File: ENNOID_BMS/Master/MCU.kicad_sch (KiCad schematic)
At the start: 36 parts, among them J17 DEBUG, Q27 BSS138, U11 LTC6820, U17 STM32F303CCTx, U2 LTC6820, Y1 8MHz

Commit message: ENNOID BMS PCBs completed
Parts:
- Q27: footprint TO_SOT_Packages_SMD:SOT-23 -> Package_TO_SOT_SMD:SOT-23
- U11, U2: footprint Housings_SSOP:MSOP-16_3x4mm_Pitch0.5mm -> Package_SO:MSOP-16_3x4.039mm_P0.5mm
- U17: footprint Housings_QFP:LQFP-48_7x7mm_Pitch0.5mm -> Package_QFP:LQFP-48_7x7mm_P0.5mm
- Y1: footprint Crystals:Crystal_SMD_Abracon_ABM3-2pin_5.0x3.2mm -> Crystal:Crystal_SMD_Abracon_ABM3-2Pin_5.0x3.2mm
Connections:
- net CS_TEMP: now reaches U17.25 (PB12/ADC4_IN3/COMP3_INM/I2C2_SMBA/I2S2_WS/OPAMP4_VOUT/SPI2_NSS/TIM1_BKIN/TSC_G6_IO2/USART3_CK)
- net CS_TEMP: now also U11.5 (CSB)
- net MA renamed MA_CELL
- net MA_CELL: no longer TR4.6
- net PA renamed PA_CELL
- net PA_CELL: no longer TR4.4
- net SS renamed CS_CELL
- net CS_CELL: no longer U11.5 (CSB)
- new net MA_TEMP: TR4.6
- new net PA_TEMP: TR4.4
- no-connect marks 5 -> 4
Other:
- moved on the sheet: R37, R51

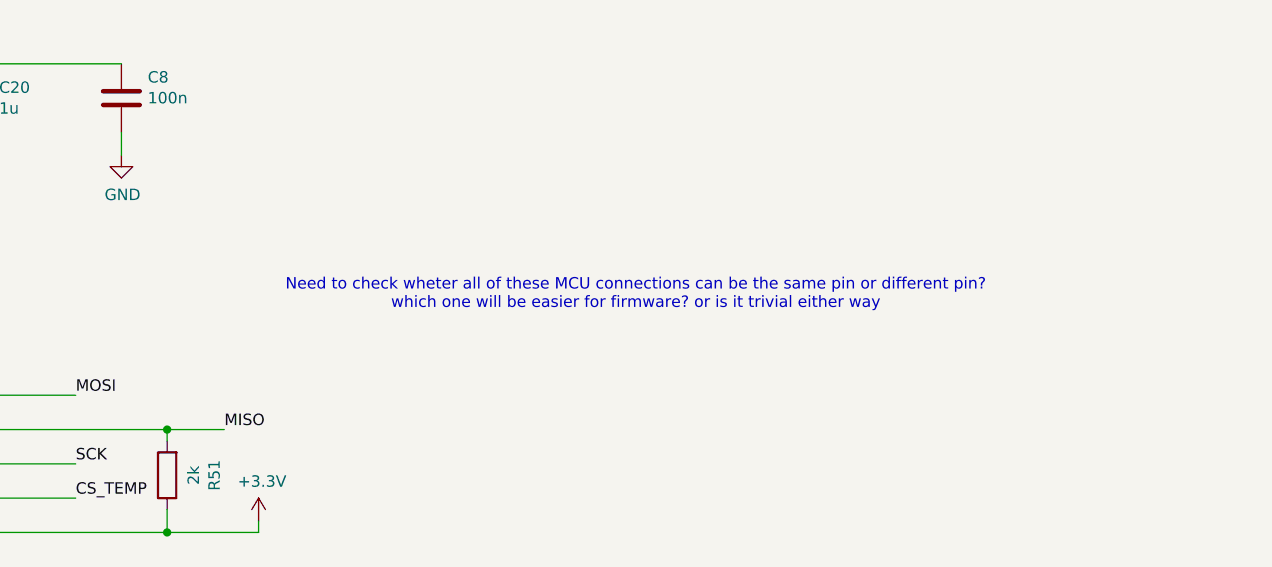
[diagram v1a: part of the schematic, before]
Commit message: bms architecture notes made re charging and discharging
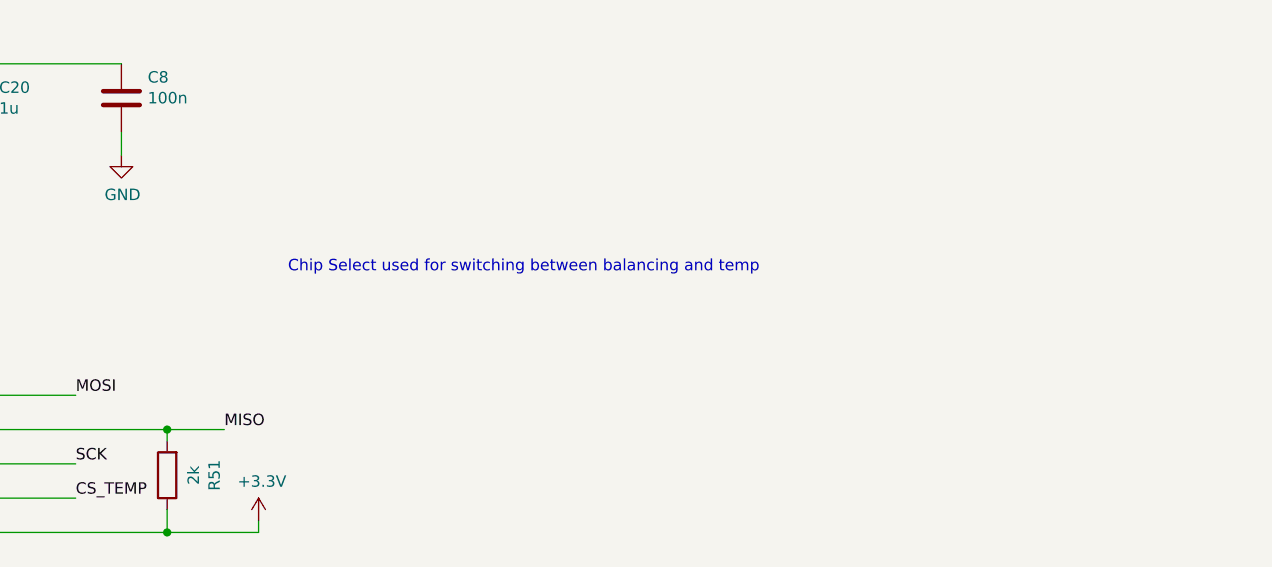
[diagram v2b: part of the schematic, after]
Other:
- note added: "Chip Select used for switching between balancing and temp"
- note removed: "Need to check wheter all of these MCU connections can be the same pin or different pin? which one will be easier for firmware? or is it trivial either way"
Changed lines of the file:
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@@
 		)
 	)
-	(text "Need to check wheter all of these MCU connections can be the same pin or different pin?\nwhich one will be easier for firmware? or is it trivial either way"
+	(text "Chip Select used for switching between balancing and temp"
 		(exclude_from_sim no)
-		(at 510.54 113.284 0)
+		(at 498.094 110.236 0)
 		(effects
 			(font

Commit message: Slave with SMD and no other fuses
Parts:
- removed C84: 100n, Capacitor_SMD:C_0603_1608Metric, symbol BMS-Master-rescue:C-Device-BMS-Master-rescue
- removed R170: 100k, Resistor_SMD:R_0603_1608Metric, symbol BMS-Master-rescue:R-Device-BMS-Master-rescue
- J15: renamed from J17; footprint Connector_Molex:Molex_PicoBlade_53398-0571_1x05-1MP_P1.25mm_Vertical -> Connector_JST:JST_XH_B5B-XH-A_1x05_P2.50mm_Vertical; MPN 53398-0571 -> B5B-XH-A
- renumbered C76 to C42, C77 to C43, C78 to C44, C6 to C45, C23 to C46, C7 to C47, C24 to C48, C20 to C49, C25 to C50, C8 to C51, C26 to C52, C80 to C53, C81 to C54, C82 to C55, C83 to C56, Q27 to Q5, R168 to R66, R5 to R67, R12 to R68, R6 to R69, R7 to R70, R18 to R71, R48 to R72, R36 to R73, R49 to R74, R37 to R75, R51 to R76, TR2 to TR3, U17 to U12, U2 to U13, U11 to U14
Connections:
- net +3.3V is gone; now on net +3V3: C49.2, C50.2, C51.1, C52.1, R75.1, R76.1, U13.1 (EN), U13.12 (MSTR), U13.6 (Vcc0), U13.7 (POL), U13.8 (PHA), U13.9 (VCC), U14.1 (EN), U14.12 (MSTR), U14.6 (Vcc0), U14.7 (POL), U14.8 (PHA), U14.9 (VCC)
- net BUZZER: no longer names the net of U12.38 (ADC1_EXTI15/ADC2_EXTI15/I2C1_SCL/I2S3_WS/SPI1_NSS/SPI3_NSS/SYS_JTDI/TIM1_BKIN/TIM2_CH1/TIM2_ETR/TIM8_CH1/USART2_RX/PA15)
- net ChargeEnable renamed Charge_enable
- net CoolingEnable renamed Charger_Safey
- net DischargeNegEnable: no longer names the net of U12.4 (PC15/ADC1_EXTI15/ADC2_EXTI15/RCC_OSC32_OUT)
- net DischargePosEnable renamed Discharge_enable
- net NTC_Switch: no longer names the net of U12.10 (ADC1_IN1/COMP1_INM/COMP1_OUT/COMP7_INP/RTC_TAMP2/SYS_WKUP1/TIM2_CH1/TIM2_ETR/TIM8_BKIN/TIM8_ETR/TSC_G1_IO1/USART2_CTS/PA0)
- net OLED_RST: no longer names the net of U12.45 (PB8/CAN_RX/COMP1_OUT/I2C1_SCL/TIM16_CH1/TIM1_BKIN/TIM4_CH3/TIM8_CH2/TSC_SYNC)
- net OLED_SCL: no longer names the net of U12.42 (PB6/I2C1_SCL/TIM16_CH1N/TIM4_CH1/TIM8_BKIN2/TIM8_CH1/TIM8_ETR/TSC_G5_IO3/USART1_TX)
- net OLED_SDA: no longer names the net of U12.43 (PB7/I2C1_SDA/TIM17_CH1N/TIM3_CH4/TIM4_CH2/TIM8_BKIN/TSC_G5_IO4/USART1_RX)
- net PreChargeEnable renamed Multipurpose_enable
- net Safety: no longer names the net of U12.2 (PC13/RTC_OUT_ALARM/RTC_OUT_CALIB/RTC_TAMP1/RTC_TS/SYS_WKUP2/TIM1_CH1N)

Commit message: fuse boards
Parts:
- C45, C46, C47, C48: MPN GRM188R71H103KA01D -> 885012206114
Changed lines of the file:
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@@
 			)
 		)
-		(property "MPN" "GRM188R71H103KA01D"
+		(property "MPN" "885012206114"
 			(at 375.92 49.53 0)
 			(effects
@@
 			)
 		)
-		(property "MPN" "GRM188R71H103KA01D"
+		(property "MPN" "885012206114"
 			(at 361.95 49.53 0)
 			(effects
@@
 			)
 		)
-		(property "MPN" "GRM188R71H103KA01D"
+		(property "MPN" "885012206114"
 			(at 363.22 119.38 0)
 			(effects
@@
 			)
 		)
-		(property "MPN" "GRM188R71H103KA01D"
+		(property "MPN" "885012206114"
 			(at 377.19 119.38 0)
 			(effects
